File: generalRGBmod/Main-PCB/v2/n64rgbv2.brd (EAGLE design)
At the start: 50.5 x 31.1 mm, 77 parts, among them J3 2510-, U1 5M570ZT100C5, U2 ADV7125/ADV7123, U4 TLV70018-DDC

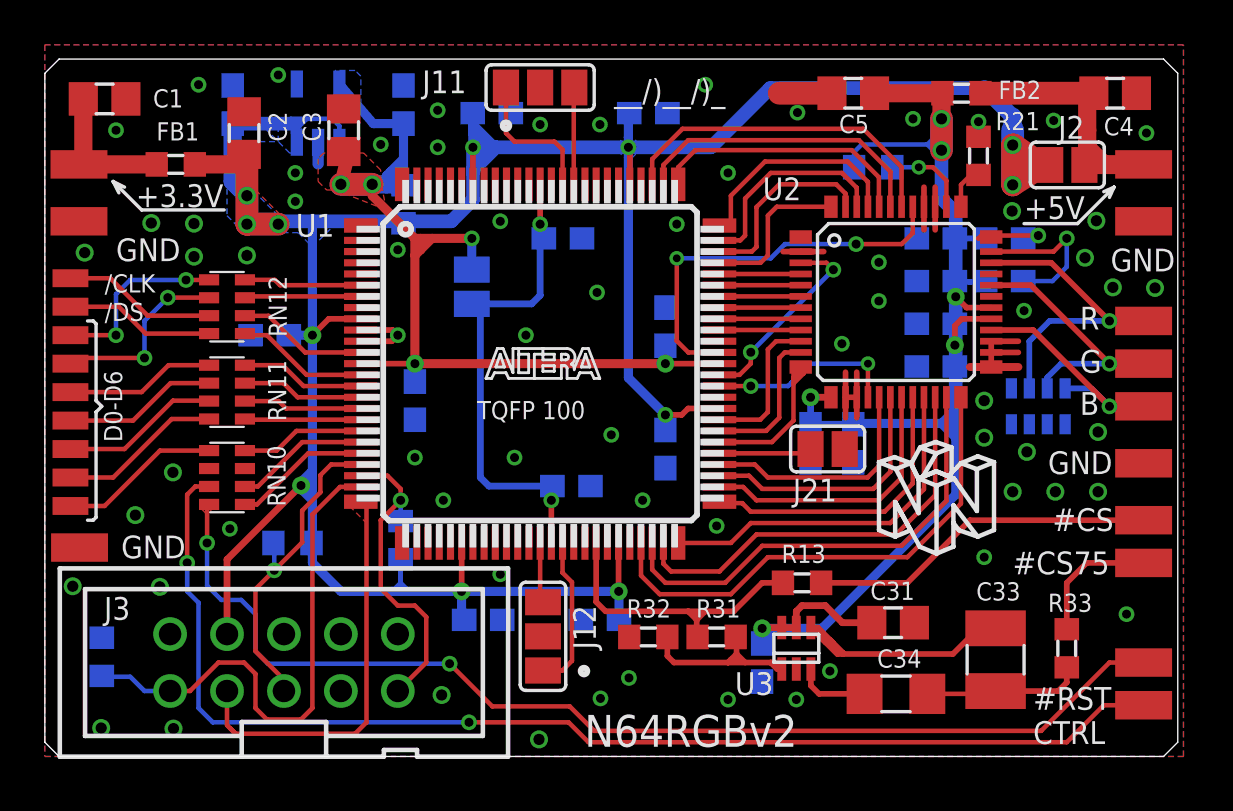
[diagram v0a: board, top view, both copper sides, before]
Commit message: PCB Update: remove jumper for analog power supply I recommend 5V for the analog part anyway. So now the user is forced to use 5V here!
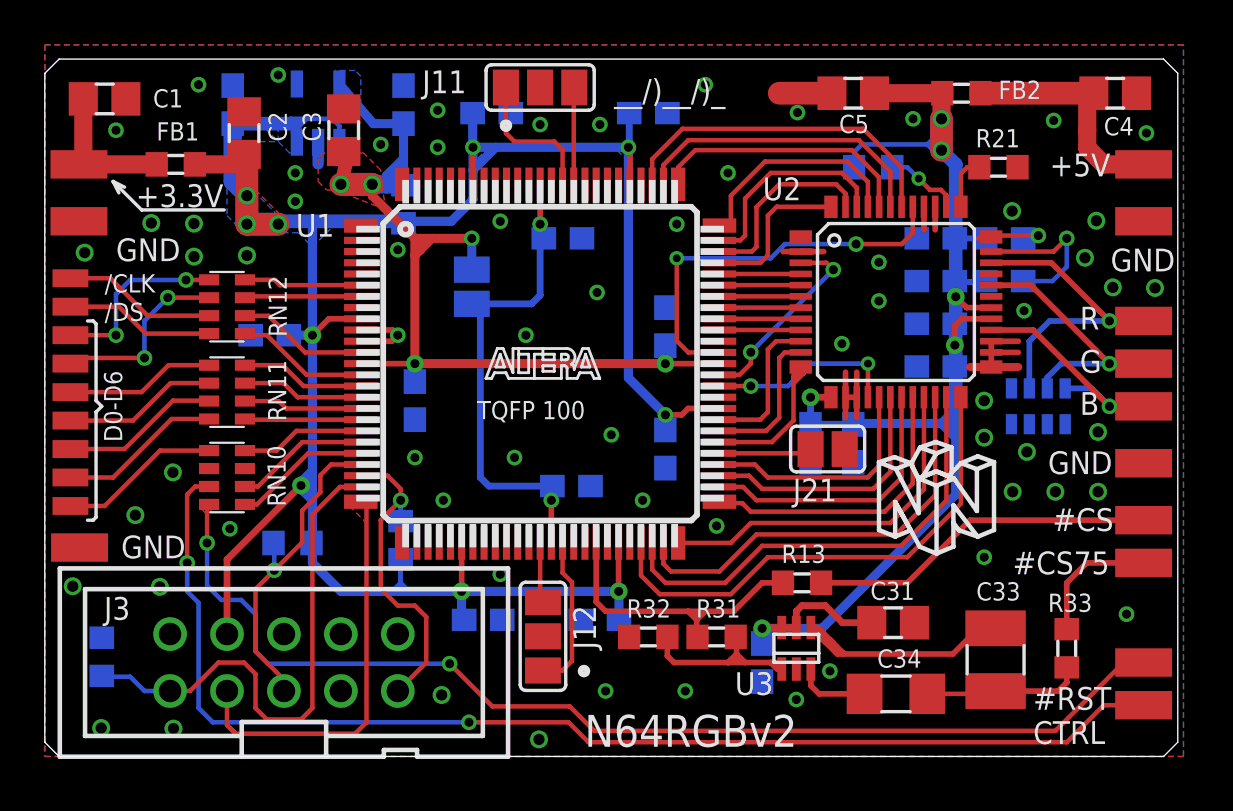
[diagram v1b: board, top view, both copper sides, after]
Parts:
- removed J2: (no value), jumper:SJ
- moved R21 1.02 mm to (42.5, 26.3), turned to 0 degrees
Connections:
- net N$44: no longer J2.2
- net VCC@3.3V: no longer J2.1
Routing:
- net VCC@3.3V: track 147.3 -> 116.8 mm, vias 12 -> 10
- net N$44: track 12.5 -> 10.7 mm
- net GND: track 23.3 -> 21.6 mm, vias 67 -> 65
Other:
- board text added: "N64RGBv2_20180205"
- board text added: "PCB Design (c) 2017-2018 Peter Bartmann"
- board text removed: "J2"
- board text removed: "N64RGBv2_20180121"

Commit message: pcb update: add some additional pads for rst and ctrl io
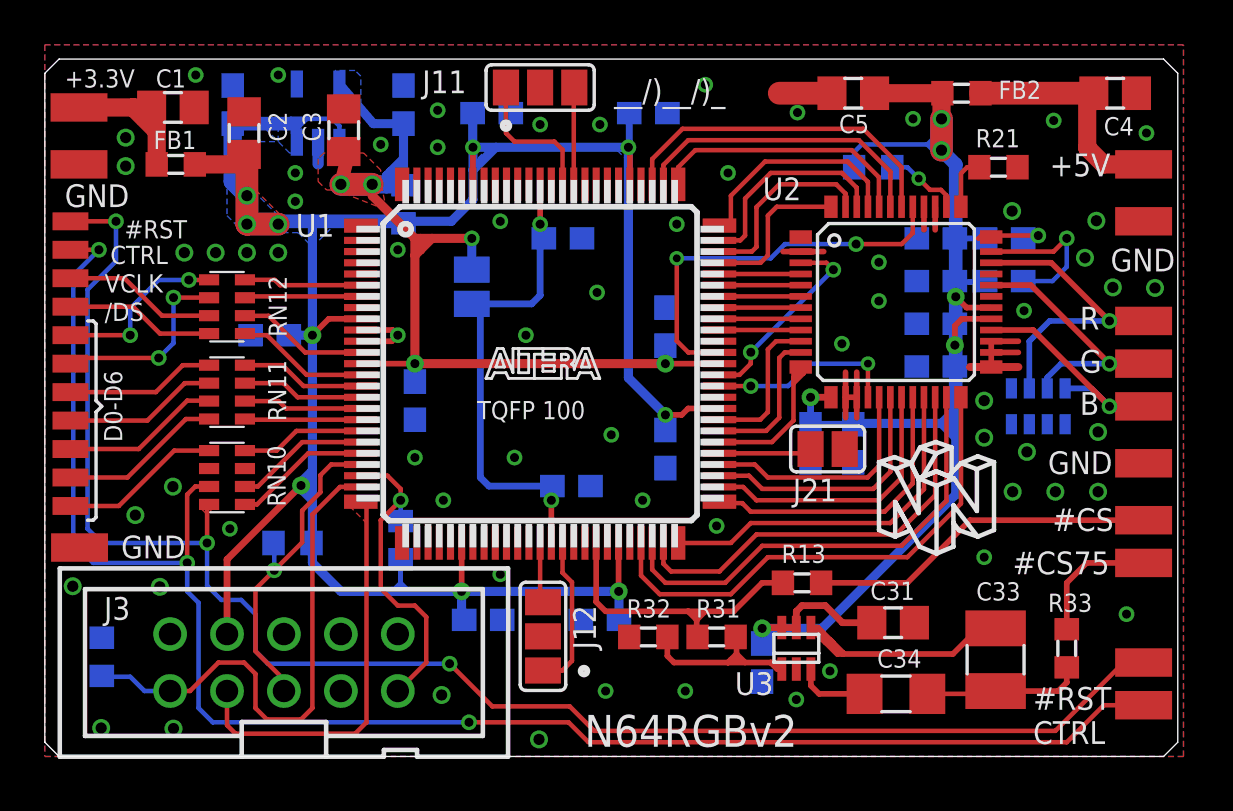
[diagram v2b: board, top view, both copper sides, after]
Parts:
- added CTRL_A, RST#_A: SMD1, wirepad:SMD0,8-1,6
- moved C1 3.07 mm to (5.71, 29.0)
- moved P_GND0 2.54 mm to (1.52, 26.4)
- moved P_VCC0 2.54 mm to (1.52, 29.0)
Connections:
- net N$5: now also RST#_A.P$1
- net N$6: now also CTRL_A.P$1
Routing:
- net N$5: track 50.4 -> 72.2 mm, vias 2 -> 3
- net N$6: track 54.3 -> 74.6 mm, vias 2 -> 3
- net N$54: track 6.62 -> 7.31 mm
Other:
- board text added: "N64RGBv2_20190105"
- board text added: "PCB Design (c) 2017-2019 Peter Bartmann"
- board text added: "VCLK"
- board text removed: "/CLK"
- board text removed: "N64RGBv2_20180205"
- board text removed: "PCB Design (c) 2017-2018 Peter Bartmann"
